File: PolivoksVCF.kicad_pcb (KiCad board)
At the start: 2 copper layers, 29.6 x 106.5 mm, 48 parts, among them J1 CV1, J2 CV2, J3 IN, J5 OUT, Q1 2N3904, SW1 SW_SPDT, U1 TL072, U2 LM4250, U3 LM4250

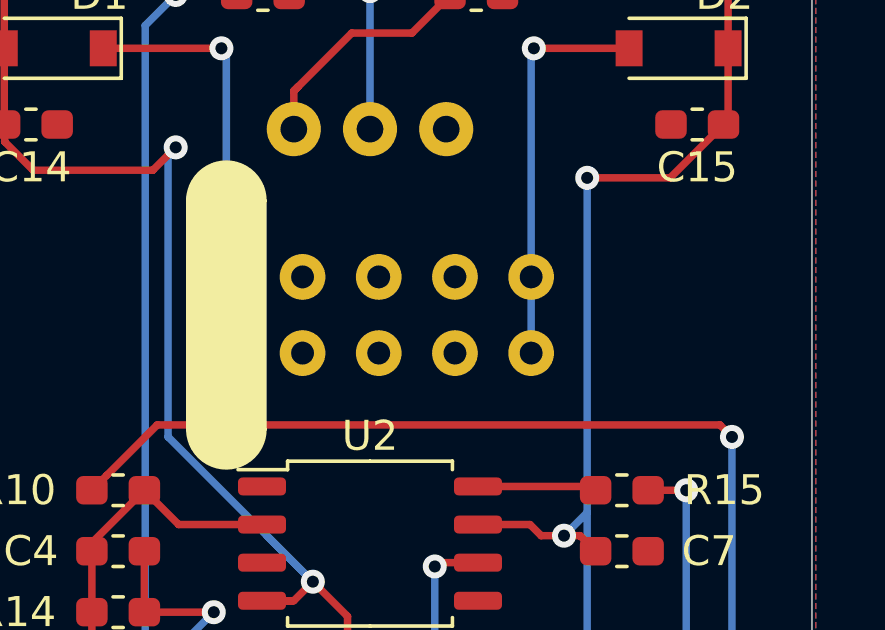
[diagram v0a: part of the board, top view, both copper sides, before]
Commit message: Small fix around power connector
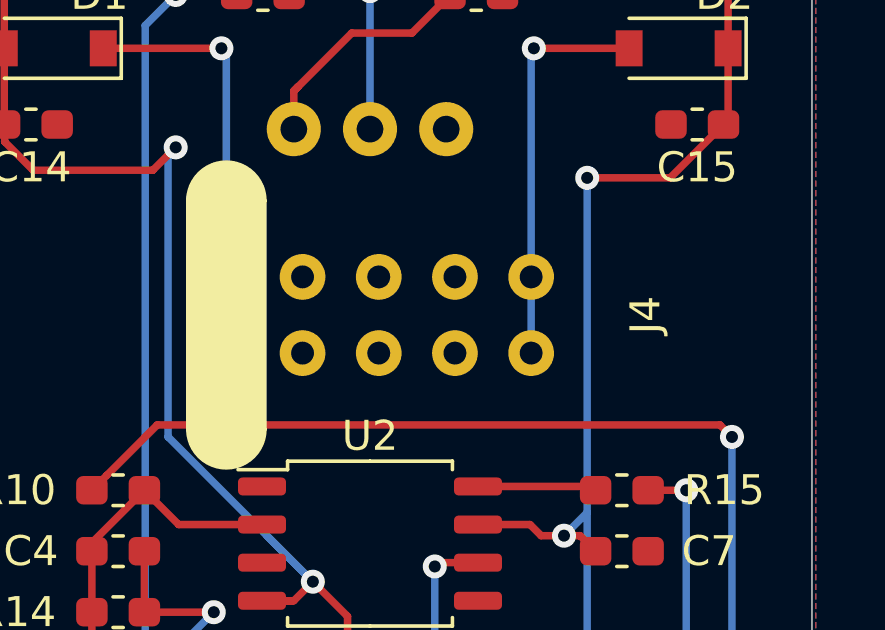
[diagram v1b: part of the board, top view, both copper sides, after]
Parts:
- C8, C9: value CP -> 10u
- renumbered ~ to J4
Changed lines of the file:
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@@
-(kicad_pcb (version 20171130) (host pcbnew 5.1.4)
+(kicad_pcb (version 20171130) (host pcbnew "(5.1.5)-3")
   (general
     (thickness 1.6)
     (drawings 10)
-    (tracks 293)
+    (tracks 294)
     (zones 0)
     (modules 48)
@@
     (solder_mask_min_width 0.25)
     (aux_axis_origin 0 0)
-    (visible_elements FFFFFF7F)
+    (visible_elements 7FFFFFFF)
     (pcbplotparams
       (layerselection 0x010fc_ffffffff)
@@
       (effects (font (size 1 1) (thickness 0.15)))
     )
-    (fp_text value CP (at 0 5.2 90) (layer F.Fab)
+    (fp_text value 10u (at 0 5.2 90) (layer F.Fab)
       (effects (font (size 1 1) (thickness 0.15)))
     )
@@
       (effects (font (size 1 1) (thickness 0.15)))
     )
-    (fp_text value CP (at 0 5.2 90) (layer F.Fab)
+    (fp_text value 10u (at 0 5.2 90) (layer F.Fab)
       (effects (font (size 1 1) (thickness 0.15)))
     )
@@
   (module Kraakenstuff:EuroHeader10 (layer F.Cu)
     (at 266.102501 41.656 90)
-    (fp_text reference ~ (at 0 8.89 90) (layer F.SilkS)
+    (fp_text reference J4 (at 0 8.89 90) (layer F.SilkS)
       (effects (font (size 1 1) (thickness 0.15)))
     )
@@
   (via (at 260.858 32.766) (size 0.8) (drill 0.4) (layers F.Cu B.Cu) (net 12))
   (segment (start 260.858 32.766) (end 256.92 32.766) (width 0.25) (layer F.Cu) (net 12))
-  (segment (start 261.022501 40.386) (end 261.022501 42.926) (width 0.25) (layer B.Cu) (net 12))
+  (segment (start 261.022501 41.914) (end 261.022501 40.386) (width 0.25) (layer B.Cu) (net 12))
+  (segment (start 261.022501 42.926) (end 261.022501 41.914) (width 0.25) (layer B.Cu) (net 12))
   (segment (start 261.022501 32.930501) (end 260.858 32.766) (width 0.25) (layer B.Cu) (net 12))
   (segment (start 261.022501 40.386) (end 261.022501 32.930501) (width 0.25) (layer B.Cu) (net 12))
@@
   (segment (start 274.448 32.766) (end 271.272 32.766) (width 0.25) (layer F.Cu) (net 13))
   (segment (start 271.272 40.296501) (end 271.182501 40.386) (width 0.25) (layer B.Cu) (net 13))
-  (segment (start 271.182501 40.386) (end 271.182501 42.926) (width 0.25) (layer B.Cu) (net 13))
+  (segment (start 271.182501 42.926) (end 271.182501 40.386) (width 0.25) (layer B.Cu) (net 13))
   (segment (start 271.182501 32.855499) (end 271.272 32.766) (width 0.25) (layer B.Cu) (net 13))
   (segment (start 271.182501 40.386) (end 271.182501 32.855499) (width 0.25) (layer B.Cu) (net 13))
